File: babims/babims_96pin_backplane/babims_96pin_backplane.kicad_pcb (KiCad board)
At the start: 2 copper layers, 2 parts

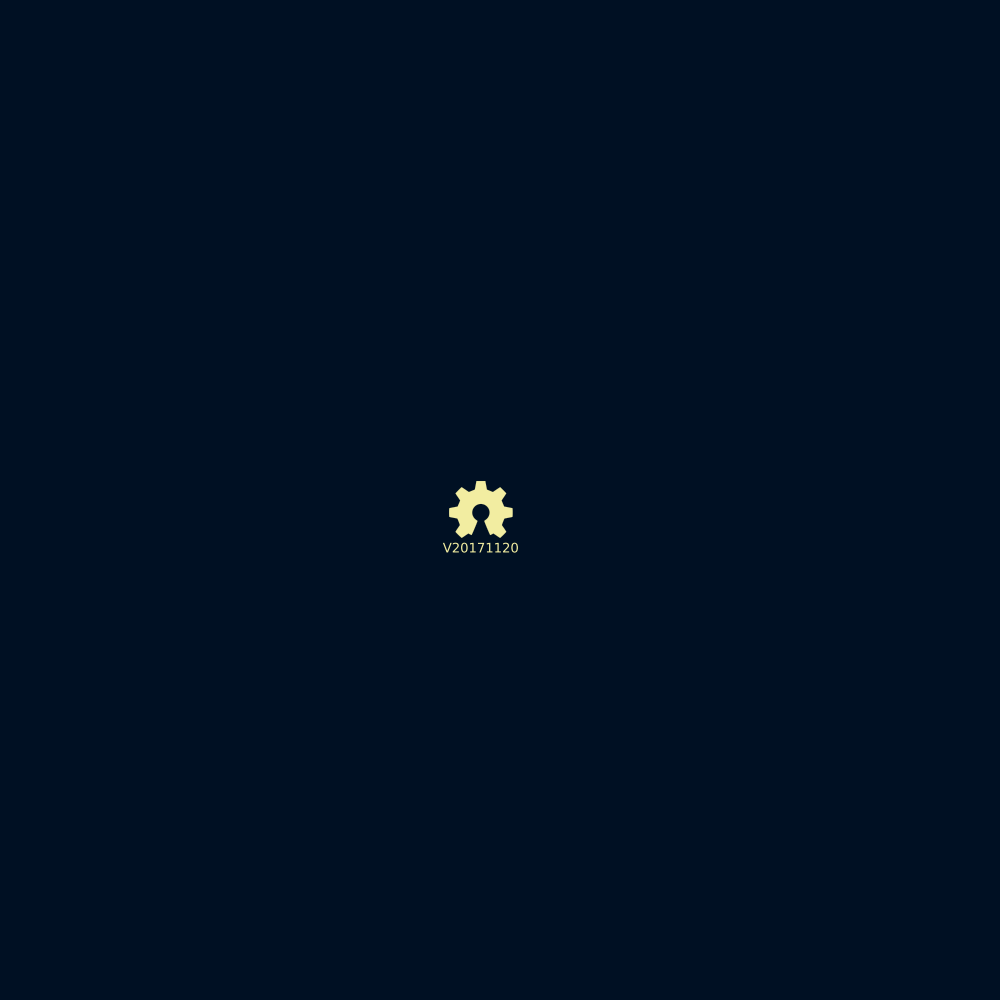
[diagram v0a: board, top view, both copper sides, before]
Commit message: * first definition of the connection nets
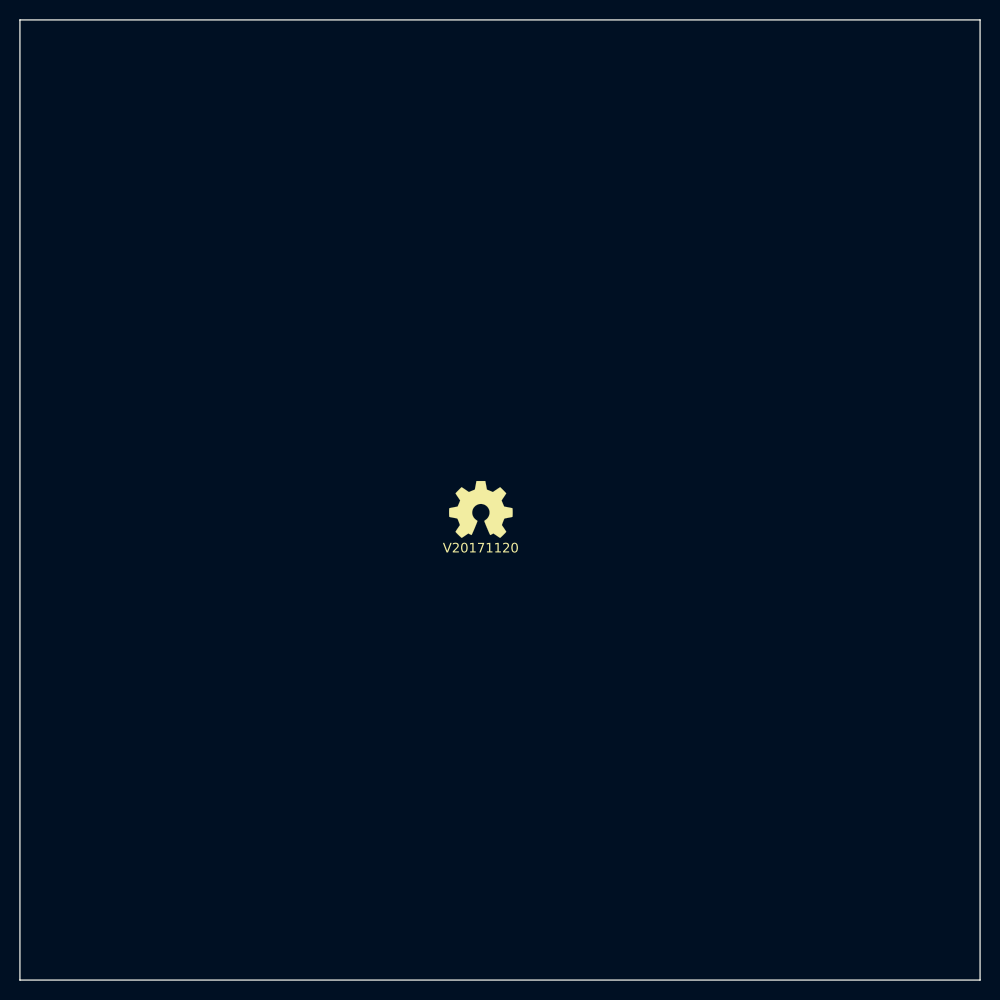
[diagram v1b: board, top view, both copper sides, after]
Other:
- board outline added: 100 x 100 mm
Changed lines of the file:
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@@
     (area 143.609505 97.866906 152.473829 108.0274)
     (thickness 1.6)
-    (drawings 0)
+    (drawings 4)
     (tracks 0)
     (zones 0)
@@
     )
   )
+  (gr_line (start 100 150) (end 100 50) (layer Edge.Cuts) (width 0.15))
+  (gr_line (start 200 150) (end 100 150) (layer Edge.Cuts) (width 0.15))
+  (gr_line (start 200 50) (end 200 150) (layer Edge.Cuts) (width 0.15))
+  (gr_line (start 100 50) (end 200 50) (layer Edge.Cuts) (width 0.15))
 )
